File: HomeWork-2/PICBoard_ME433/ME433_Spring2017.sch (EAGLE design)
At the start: 13 parts, among them J6 USB_MINI-B_SMT, Q1 MCP1702

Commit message: Schematic Version #1
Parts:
- removed C1: (no value), ME433_Spring2017:C-US025-025X050
- removed C2: (no value), ME433_Spring2017:CPOL-USB45181B
- removed IC1: (no value), ME433_Spring2017:PIC-3
- removed J1: (no value), ME433_Spring2017:BUTTONS
- removed J2: (no value), ME433_Spring2017:CONN_08"
- removed J3: (no value), ME433_Spring2017:CONN_16
- removed J4: (no value), ME433_Spring2017:SLIDER_SWITCH
- removed J5: (no value), ME433_Spring2017:USB_GREENBOARD_PULLOUT
- removed LED1: (no value), ME433_Spring2017:LEDSFH482
- removed Q1: MCP1702, ME433_Spring2017:MCP1702
- removed QF1: OSC_8MHZ7A-12.5KHZ, ME433_Spring2017:OSC_8MHZ7A-12.5KHZ
- removed R1: (no value), ME433_Spring2017:R-US_0204/7
- added 0.1U1, 0.1U4, 0.1U5, CRY_1, CRY_2, VDD_GND: 0.1u, ME433_Spring2017:C-US025-025X050
- added 10K_2, 10K_3, PB_PULLDOWN, RST_PULLUP: 10k, ME433_Spring2017:R-US_0204/7
- added CONN_16_A, CONN_16_A1: (no value), ME433_Spring2017:CONN_16
- added CONN_8_A, CONN_8_A1: (no value), ME433_Spring2017:CONN_08"
- added CRYSTAL_8MHZ: OSC_8MHZ7A-12.5KHZ, ME433_Spring2017:OSC_8MHZ7A-12.5KHZ
- added CRY_TANTALUM, VCAP: 10u, ME433_Spring2017:CPOL-USB45181B
- added GREEN, RED: (no value), ME433_Spring2017:LEDSFH482
- added GREEN_LED, RED_LED: 330, ME433_Spring2017:R-US_0204/7
- added GREEN_USB_SAFETY: (no value), ME433_Spring2017:USB_GREENBOARD_PULLOUT
- added PB_LED, PB_RST: (no value), ME433_Spring2017:BUTTONS
- added PIC32MX250: (no value), ME433_Spring2017:PIC-3
- added PIC_KIT_3: (no value), ME433_Spring2017:PICKIT3NO_SILK_FEMALE_PTH
- added SLIDER_SWITCH: (no value), ME433_Spring2017:SLIDER_SWITCH
- added _: MCP1702, ME433_Spring2017:MCP1702
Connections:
- new net +3V3: 0.1U1.1, CONN_8_A.2, CRY_2.1, CRY_TANTALUM.+, PB_LED.1, PIC32MX250.13, PIC32MX250.28, PIC_KIT_3.2, RED.A, RST_PULLUP.2, _.C
- new net +5V: CONN_8_A1.7, J6.VBUS, PIC32MX250.15, SLIDER_SWITCH.1
- new net GND: 0.1U1.2, CONN_8_A.1, CONN_8_A1.8, CRYSTAL_8MHZ.2, CRY_1.1, CRY_2.2, CRY_TANTALUM.-, GREEN_LED.1, J6.GND, PB_PULLDOWN.2, PB_RST.1, PIC32MX250.19, PIC32MX250.8, PIC_KIT_3.3, RED_LED.2, SLIDER_SWITCH.3, VCAP.-, _.E
- new net N$1: CONN_8_A.8, PIC32MX250.2
- new net N$10: PB_LED.2, PB_PULLDOWN.1, PIC32MX250.11
- new net N$11: PIC32MX250.20, VCAP.+
- new net N$12: J6.D+, PIC32MX250.21
- new net N$13: J6.D-, PIC32MX250.22
- new net N$14: CRY_1.2, SLIDER_SWITCH.2, _.B
- new net N$15: PB_RST.2, PIC32MX250.1, PIC_KIT_3.1, RST_PULLUP.1
- new net N$16: RED.C, RED_LED.1
- new net N$17: CONN_8_A.7, PIC32MX250.3
- new net N$18: CONN_8_A.5, PIC32MX250.7
- new net N$2: PIC32MX250.4, PIC_KIT_3.4
- new net N$22: PIC32MX250.16
- new net N$23: CONN_8_A1.6, PIC32MX250.17
- new net N$3: PIC32MX250.5, PIC_KIT_3.5
- new net N$4: GREEN.A, PIC32MX250.12
- new net N$5: CRYSTAL_8MHZ.1, PIC32MX250.9
- new net N$6: CRYSTAL_8MHZ.3, PIC32MX250.10
- new net N$7: GREEN.C, GREEN_LED.2
- new net N$8: J6.ID, PIC32MX250.14
- new net N$9: CONN_8_A.6, PIC32MX250.6
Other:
- moved on the sheet: J6

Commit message: Schematic Version #2
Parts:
- removed 0.1U4, 0.1U5: 0.1u, ME433_Spring2017:C-US025-025X050
- removed 10K_2, 10K_3: 10k, ME433_Spring2017:R-US_0204/7
- removed CONN_16_A, CONN_16_A1: (no value), ME433_Spring2017:CONN_16
- removed GREEN_USB_SAFETY: (no value), ME433_Spring2017:USB_GREENBOARD_PULLOUT
- CONN_8_A: value (none) -> pinout_1
- CONN_8_A1: value (none) -> pinout_2
- GREEN, RED: value (none) -> led
- PB_LED: value (none) -> button_led
- PB_RST: value (none) -> reset_swtch
- PIC32MX250: value (none) -> pic
- PIC_KIT_3: value (none) -> programmer
- SLIDER_SWITCH: value (none) -> mains
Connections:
- removed net N$17: CONN_8_A.7, PIC32MX250.3
- removed net N$18 (its old number): CONN_8_A.5, PIC32MX250.7
- removed net N$22: PIC32MX250.16
- removed net N$23: CONN_8_A1.6, PIC32MX250.17
- removed net N$4 (its old number): GREEN.A, PIC32MX250.12
- removed net N$9 (its old number): CONN_8_A.6, PIC32MX250.6
- new net N$3: CONN_8_A.3, GREEN.A, PIC32MX250.12
- net +3V3: now also PIC32MX250.23, VDD_GND.1; no longer CONN_8_A.2, PIC_KIT_3.2
- net +5V: now also CONN_8_A1.2, J6.SHIELD; no longer CONN_8_A1.7
- net GND: now also CONN_8_A1.1, PIC32MX250.27, VDD_GND.2; no longer CONN_8_A1.8
- net N$1: now also CONN_8_A.2, PIC_KIT_3.2; no longer CONN_8_A.8, PIC32MX250.2
- net N$10: now also CONN_8_A.4
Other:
- moved on the sheet: CONN_8_A, CONN_8_A1, CRYSTAL_8MHZ, CRY_1, CRY_2, CRY_TANTALUM, GREEN, GREEN_LED, J6, PB_PULLDOWN, PB_RST, PIC_KIT_3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

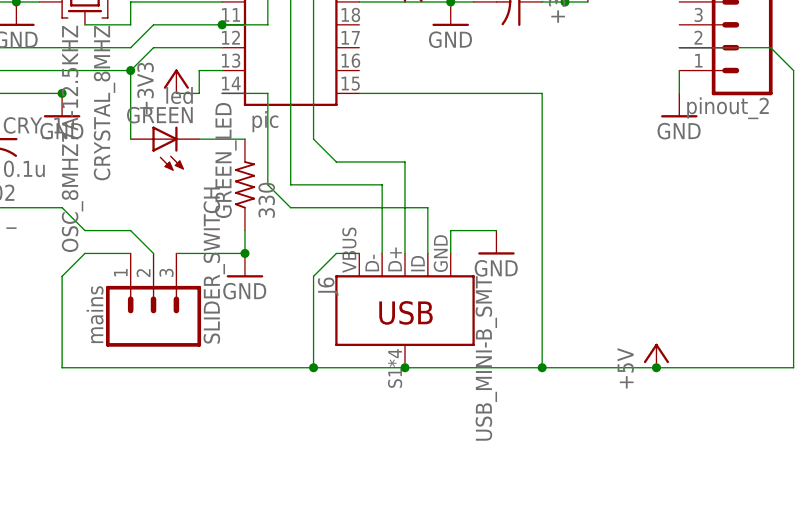
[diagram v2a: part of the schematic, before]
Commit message: Schematic Version #3 - Added PTH USB package
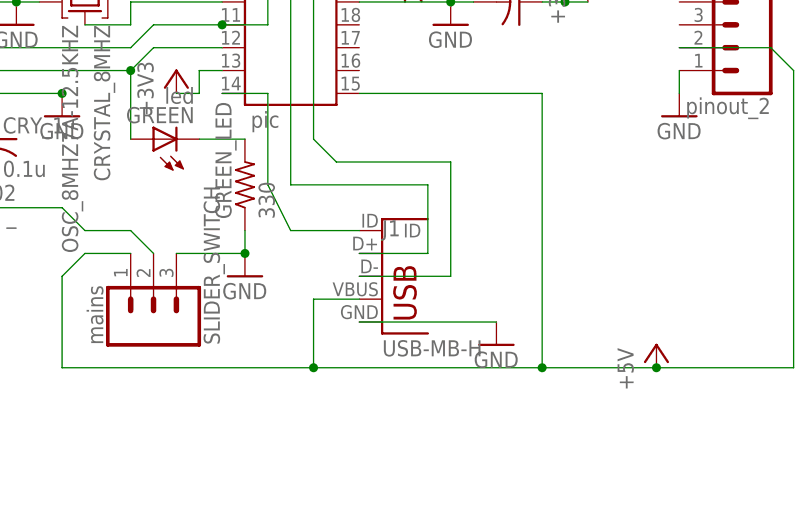
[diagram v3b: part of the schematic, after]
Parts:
- removed J6: USB_MINI-B_SMT, ME433_Spring2017:USB_MINI-B_SMT
- added J1: USB-MB-H, ME433_Spring2017:USB-MB-H
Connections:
- net +5V: now also J1.VBUS; no longer J6.SHIELD, J6.VBUS
- net GND: now also J1.GND; no longer J6.GND
- net N$18: now also J1.ID; no longer J6.ID
- net N$4: now also J1.D+; no longer J6.D-
- net N$9: now also J1.D-; no longer J6.D+
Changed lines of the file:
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@@
 <part name="RED_LED" library="ME433_Spring2017" deviceset="R-US_" device="0204/7" value="330"/>
 <part name="SLIDER_SWITCH" library="ME433_Spring2017" deviceset="SLIDER_SWITCH" device="" value="mains"/>
-<part name="J6" library="ME433_Spring2017" deviceset="USB_MINI-B" device="_SMT"/>
 <part name="RST_PULLUP" library="ME433_Spring2017" deviceset="R-US_" device="0204/7" value="10k"/>
 <part name="PB_RST" library="ME433_Spring2017" deviceset="BUTTONS" device="" value="reset_swtch"/>
@@
 <part name="+3V6" library="ME433_Spring2017" deviceset="+3V3" device=""/>
 <part name="GND8" library="ME433_Spring2017" deviceset="GND" device=""/>
+<part name="J1" library="ME433_Spring2017" deviceset="USB" device="-MB-H"/>
 </parts>
 <sheets>
@@
 <instance part="RED_LED" gate="G$1" x="43.18" y="45.72"/>
 <instance part="SLIDER_SWITCH" gate="J$1" x="83.82" y="15.24" rot="MR90"/>
-<instance part="J6" gate="G$1" x="111.76" y="17.78" rot="MR270"/>
 <instance part="RST_PULLUP" gate="G$1" x="139.7" y="101.6" rot="R270"/>
 <instance part="PB_RST" gate="G$1" x="129.54" y="93.98" rot="MR90"/>
@@
 <instance part="GND7" gate="1" x="68.58" y="48.26"/>
 <instance part="+3V6" gate="G$1" x="132.08" y="53.34"/>
-<instance part="GND8" gate="1" x="121.92" y="22.86"/>
+<instance part="GND8" gate="1" x="121.92" y="12.7"/>
+<instance part="J1" gate="G$1" x="109.22" y="15.24"/>
 </instances>
 <busses>
@@
 </segment>
 <segment>
-<pinref part="J6" gate="G$1" pin="GND"/>
-<wire x1="116.84" y1="22.86" x2="116.84" y2="25.4" width="0.1524" layer="91"/>
-<wire x1="116.84" y1="25.4" x2="121.92" y2="25.4" width="0.1524" layer="91"/>
+<pinref part="J1" gate="G$1" pin="GND"/>
 <pinref part="GND8" gate="1" pin="GND"/>
+<wire x1="106.68" y1="15.24" x2="121.92" y2="15.24" width="0.1524" layer="91"/>
 </segment>
 </net>
@@
 <junction x="139.7" y="10.16"/>
 <pinref part="SLIDER_SWITCH" gate="J$1" pin="1"/>
-<wire x1="111.76" y1="10.16" x2="127" y2="10.16" width="0.1524" layer="91"/>
 <wire x1="127" y1="10.16" x2="139.7" y2="10.16" width="0.1524" layer="91"/>
 <wire x1="81.28" y1="22.86" x2="76.2" y2="22.86" width="0.1524" layer="91"/>
@@
 <wire x1="73.66" y1="10.16" x2="101.6" y2="10.16" width="0.1524" layer="91"/>
 <pinref part="CONN_8_A1" gate="G$1" pin="2"/>
-<wire x1="101.6" y1="10.16" x2="111.76" y2="10.16" width="0.1524" layer="91"/>
+<wire x1="101.6" y1="10.16" x2="127" y2="10.16" width="0.1524" layer="91"/>
 <wire x1="142.24" y1="45.72" x2="152.4" y2="45.72" width="0.1524" layer="91"/>
 <wire x1="152.4" y1="45.72" x2="154.94" y2="43.18" width="0.1524" layer="91"/>
 <wire x1="154.94" y1="43.18" x2="154.94" y2="10.16" width="0.1524" layer="91"/>
-<pinref part="J6" gate="G$1" pin="SHIELD"/>
-<junction x="111.76" y="10.16"/>
-<pinref part="J6" gate="G$1" pin="VBUS"/>
-<wire x1="106.68" y1="22.86" x2="104.14" y2="22.86" width="0.1524" layer="91"/>
-<wire x1="104.14" y1="22.86" x2="101.6" y2="20.32" width="0.1524" layer="91"/>
-<wire x1="101.6" y1="20.32" x2="101.6" y2="10.16" width="0.1524" layer="91"/>
-<junction x="101.6" y="10.16"/>
 <pinref part="PIC32MX250" gate="G$1" pin="15"/>
 <wire x1="106.68" y1="40.64" x2="127" y2="40.64" width="0.1524" layer="91"/>
 <wire x1="127" y1="40.64" x2="127" y2="10.16" width="0.1524" layer="91"/>
 <junction x="127" y="10.16"/>
+<pinref part="J1" gate="G$1" pin="VBUS"/>
+<wire x1="106.68" y1="17.78" x2="101.6" y2="17.78" width="0.1524" layer="91"/>
+<wire x1="101.6" y1="17.78" x2="101.6" y2="10.16" width="0.1524" layer="91"/>
+<junction x="101.6" y="10.16"/>
 </segment>
 </net>
@@
 <wire x1="99.06" y1="58.42" x2="106.68" y2="58.42" width="0.1524" layer="91"/>
 <wire x1="99.06" y1="58.42" x2="99.06" y2="30.48" width="0.1524" layer="91"/>
-<wire x1="99.06" y1="30.48" x2="109.22" y2="30.48" width="0.1524" layer="91"/>
-<pinref part="J6" gate="G$1" pin="D-"/>
-<wire x1="109.22" y1="30.48" x2="109.22" y2="22.86" width="0.1524" layer="91"/>
+<wire x1="99.06" y1="30.48" x2="114.3" y2="30.48" width="0.1524" layer="91"/>
+<wire x1="114.3" y1="30.48" x2="114.3" y2="22.86" width="0.1524" layer="91"/>
+<pinref part="J1" gate="G$1" pin="D+"/>
+<wire x1="114.3" y1="22.86" x2="106.68" y2="22.86" width="0.1524" layer="91"/>
 </segment>
 </net>
@@
 <wire x1="101.6" y1="55.88" x2="101.6" y2="35.56" width="0.1524" layer="91"/>
 <wire x1="101.6" y1="35.56" x2="104.14" y2="33.02" width="0.1524" layer="91"/>
-<wire x1="104.14" y1="33.02" x2="111.76" y2="33.02" width="0.1524" layer="91"/>
-<pinref part="J6" gate="G$1" pin="D+"/>
-<wire x1="111.76" y1="33.02" x2="111.76" y2="22.86" width="0.1524" layer="91"/>
+<wire x1="104.14" y1="33.02" x2="116.84" y2="33.02" width="0.1524" layer="91"/>
+<pinref part="J1" gate="G$1" pin="D-"/>
+<wire x1="106.68" y1="20.32" x2="116.84" y2="20.32" width="0.1524" layer="91"/>
+<wire x1="116.84" y1="20.32" x2="116.84" y2="33.02" width="0.1524" layer="91"/>
 </segment>
 </net>
 <net name="N$18" class="0">
 <segment>
-<pinref part="J6" gate="G$1" pin="ID"/>
-<wire x1="114.3" y1="22.86" x2="114.3" y2="27.94" width="0.1524" layer="91"/>
-<wire x1="114.3" y1="27.94" x2="99.06" y2="27.94" width="0.1524" layer="91"/>
 <pinref part="PIC32MX250" gate="G$1" pin="14"/>
 <wire x1="91.44" y1="40.64" x2="96.52" y2="40.64" width="0.1524" layer="91"/>
 <wire x1="96.52" y1="40.64" x2="96.52" y2="30.48" width="0.1524" layer="91"/>
-<wire x1="96.52" y1="30.48" x2="99.06" y2="27.94" width="0.1524" layer="91"/>
-</segment>
-</net>
+<wire x1="96.52" y1="30.48" x2="99.06" y2="25.4" width="0.1524" layer="91"/>
+<pinref part="J1" gate="G$1" pin="ID"/>
+<wire x1="99.06" y1="25.4" x2="106.68" y2="25.4" width="0.1524" layer="91"/>
+</segment>
+</net>
